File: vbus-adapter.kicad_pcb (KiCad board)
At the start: 2 copper layers, 76.5 x 49 mm, 32 parts, among them J1 VBUS, J2 CAN, J3 Screw_Terminal_01x03, J4 Screw_Terminal_01x03, J6 Backup GPIO, T800 AO3400A, U1 ISO7721D, U3 MCP2562-E-SN, U4 WeMos_S2_mini

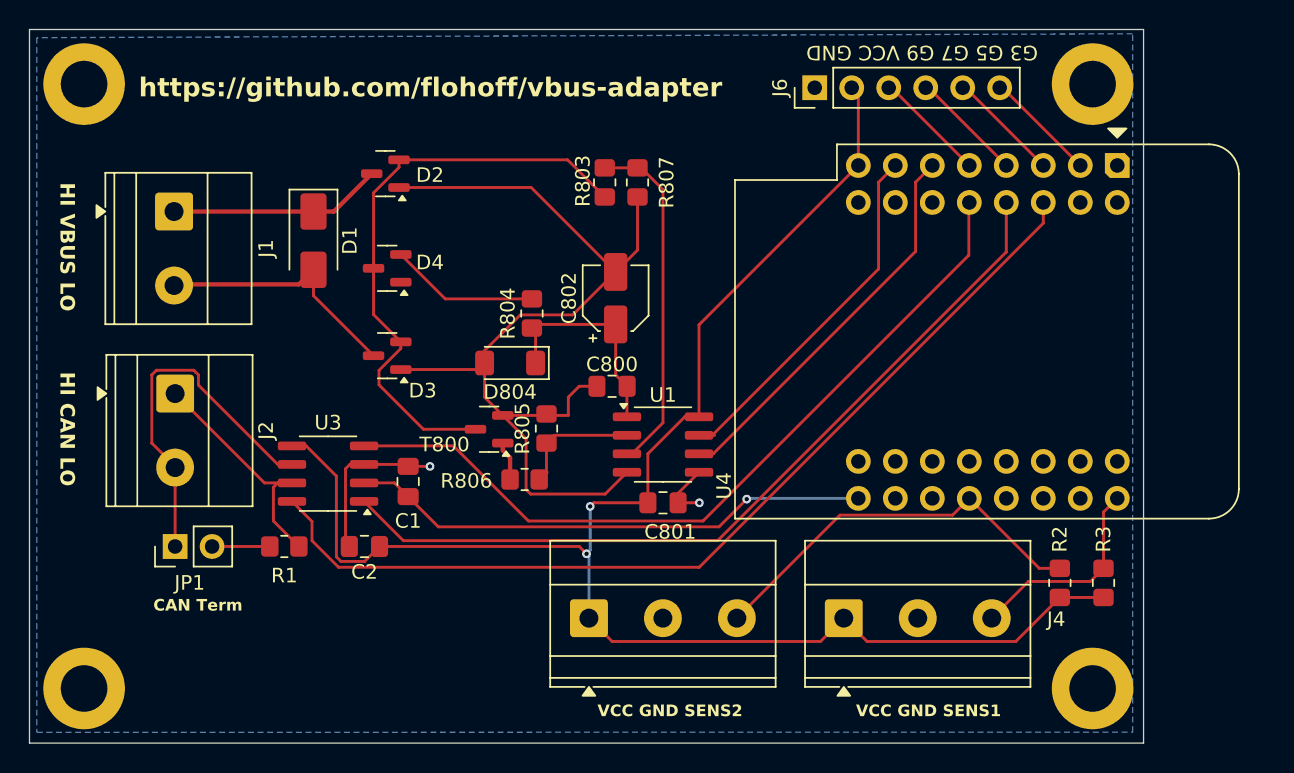
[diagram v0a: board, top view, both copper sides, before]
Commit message: Fix some issues
- Use ISO7721FDR (Default Low output) so on disconnect of
  the ESP32 (Power loss) the VBUS will not be pulled to low
  e.g. bus disabled.
- Add pull-down resistor to ISO input for TX
- Add VBUS r/w jumper disconnecting the MOSFet drain from the VBUS
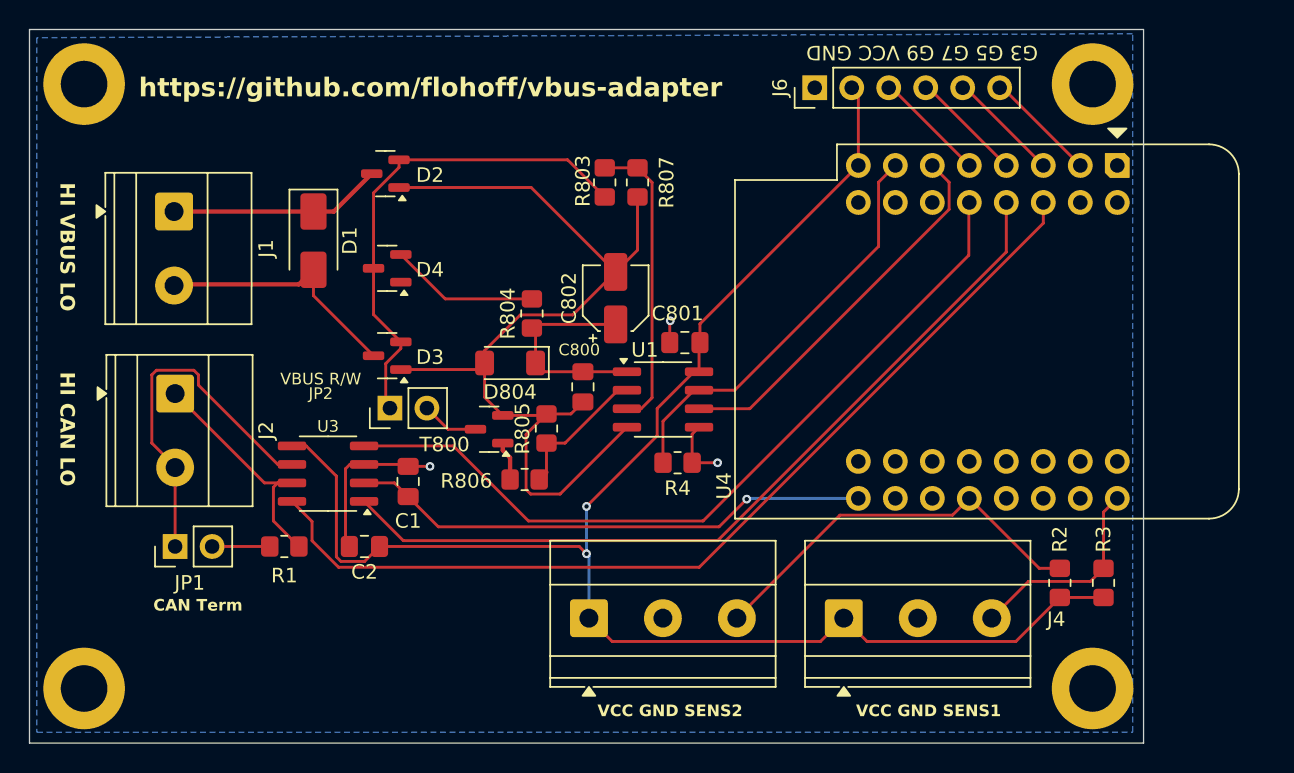
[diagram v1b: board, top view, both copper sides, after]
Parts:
- added JP2: VBUS R/W, Connector_PinHeader_2.54mm:PinHeader_1x02_P2.54mm_Vertical, F.Cu at (133.8, 99.0)
- added R4: 6k8, Resistor_SMD:R_0805_2012Metric_Pad1.20x1.40mm_HandSolder, F.Cu at (153.5, 102.8)
- U1: value ISO7721D -> ISO7721FDR
- moved C801 11.1 mm to (154.0, 94.5), turned to 180 degrees
- moved U1 3.09 mm to (152.5, 98.4)
- moved C800 2.00 mm to (147.0, 97.5), turned to -90 degrees
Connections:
- T800 pad 3: Net-(D2-K) -> Net-(JP2-B)
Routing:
- net Net-(D2-K): track 40.6 -> 34.3 mm
- net Net-(JP2-B): track 0.00 -> 3.94 mm
- net VBUS-IN: track 24.0 -> 20.5 mm
- net VBUS-MC-TX: track 25.7 -> 28.7 mm
- net VCC: track 113.1 -> 110.6 mm
- net GND: track 15.6 -> 17.3 mm, vias 2 -> 3
- net VBUS-OUT: track 9.15 -> 10.4 mm
- net VBUS-GND: track 66.7 -> 65.8 mm
- net VBUS-MC-RX: track 27.0 -> 26.3 mm

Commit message: Version 2
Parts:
- removed U4: WeMos_S2_mini, flo:WEMOS_S2_mini
- added C3: 10uF, Capacitor_SMD:C_0805_2012Metric_Pad1.18x1.45mm_HandSolder, F.Cu at (157.2, 77.2)
- added C4: 0.1uF, Capacitor_SMD:C_0805_2012Metric_Pad1.18x1.45mm_HandSolder, F.Cu at (154.7, 77.2)
- added C5: 0.1uF, Capacitor_SMD:C_0805_2012Metric_Pad1.18x1.45mm_HandSolder, F.Cu at (156.4, 82.0)
- added C6: 10uF, Capacitor_SMD:C_0805_2012Metric_Pad1.18x1.45mm_HandSolder, F.Cu at (161.4, 82.0)
- added C7: 10nF, Capacitor_SMD:C_0805_2012Metric_Pad1.18x1.45mm_HandSolder, F.Cu at (158.9, 82.0)
- added J5: Power, TerminalBlock_Phoenix:TerminalBlock_Phoenix_MPT-0,5-2-2.54_1x02_P2.54mm_Horizontal, F.Cu at (119.3, 115.1)
- added J7: Program, Connector_PinHeader_2.54mm:PinHeader_1x05_P2.54mm_Vertical, F.Cu at (154.4, 108.7)
- added Q1: SS8050, Package_TO_SOT_SMD:SOT-23, F.Cu at (167.8, 112.4)
- added Q2: SS8050, Package_TO_SOT_SMD:SOT-23, F.Cu at (158.2, 112.5)
- added R5: 10K, Resistor_SMD:R_0805_2012Metric_Pad1.20x1.40mm_HandSolder, F.Cu at (164.4, 112.6)
- added R6: 10K, Resistor_SMD:R_0805_2012Metric_Pad1.20x1.40mm_HandSolder, F.Cu at (161.8, 112.6)
- added U2: ESP32-S2-SOLO, PCM_Espressif:ESP32-S2-SOLO, F.Cu at (175.7, 93.8)
- added U5: SPX3819M5-L-3-3, Package_TO_SOT_SMD:SOT-23-5, F.Cu at (160.7, 77.3)
- J1, J2: footprint TerminalBlock_Phoenix:TerminalBlock_Phoenix_MKDS-1,5-2-5.08_1x02_P5.08mm_Horizontal -> TerminalBlock_Phoenix:TerminalBlock_Phoenix_MPT-0,5-2-2.54_1x02_P2.54mm_Horizontal
- J3: value Screw_Terminal_01x03 -> Sens 2; footprint TerminalBlock_Phoenix:TerminalBlock_Phoenix_MKDS-1,5-3-5.08_1x03_P5.08mm_Horizontal -> TerminalBlock_Phoenix:TerminalBlock_Phoenix_MPT-0,5-3-2.54_1x03_P2.54mm_Horizontal
- J4: value Screw_Terminal_01x03 -> Sens 1; footprint TerminalBlock_Phoenix:TerminalBlock_Phoenix_MKDS-1,5-3-5.08_1x03_P5.08mm_Horizontal -> TerminalBlock_Phoenix:TerminalBlock_Phoenix_MPT-0,5-3-2.54_1x03_P2.54mm_Horizontal
- moved R3 43.3 mm to (139.7, 115.3)
- moved R2 43.1 mm to (136.9, 115.3)
- moved J6 40.3 mm to (163.7, 117.3)
- moved C2 27.2 mm to (128.4, 81.5), turned to 0 degrees
- moved J4 21.7 mm to (143.3, 115.1)
- moved D2 21.1 mm to (129.3, 103.6)
- moved J3 19.7 mm to (127.8, 115.1)
- moved R1 18.9 mm to (122.4, 90.0), turned to 90 degrees
- moved C1 18.5 mm to (133.8, 85.6)
- moved U3 18.1 mm to (128.1, 85.5)
- moved J1 17.7 mm to (116.6, 103.1)
- moved JP1 17.7 mm to (116.6, 91.0)
- moved D1 17.3 mm to (124.4, 104.3)
- moved J2 13.9 mm to (116.5, 84.3)
- moved D3 12.6 mm to (129.4, 107.3)
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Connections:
- J6 pad 3: GPIO9 -> EXT1
- J6 pad 4: GPIO7 -> EXT2
- J6 pad 5: GPIO5 -> EXT3
- J6 pad 6: GPIO3 -> EXT4
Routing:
- net +5V: track 36.0 -> 107.6 mm, vias 1 -> 0
- net GND: track 17.3 -> 82.5 mm, vias 3 -> 8
- net VCC: track 110.6 -> 171.0 mm, vias 2 -> 3
- net EN: track 0.00 -> 37.3 mm, vias 0 -> 2
- net PROG_RXD: track 0.00 -> 25.4 mm, vias 0 -> 1
- net PROG_TXD: track 0.00 -> 24.2 mm, vias 0 -> 1
- net GPIO-SENS1: track 14.3 -> 36.7 mm
- net PROG: track 0.00 -> 20.6 mm
- net EXT1: track 0.00 -> 15.8 mm
- net EXT4: track 0.00 -> 15.3 mm
- net EXT2: track 0.00 -> 15.3 mm
- net EXT3: track 0.00 -> 14.8 mm
- net VBUS-MC-TX: track 28.7 -> 15.2 mm
- net GPIO-SENS2: track 27.6 -> 39.8 mm
- net VBUS-MC-RX: track 26.3 -> 15.0 mm
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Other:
- board text added: "${PROJECTNAME} ${REVISION} ${ISSUE_DATE}"
- board text added: "+5V GND"
- board text added: "GND RX TX RTS DTR"
- board text added: "GND VCC E1 E2 E3 E4"
- board text removed: "G3 G5 G7 G9 VCC GND"

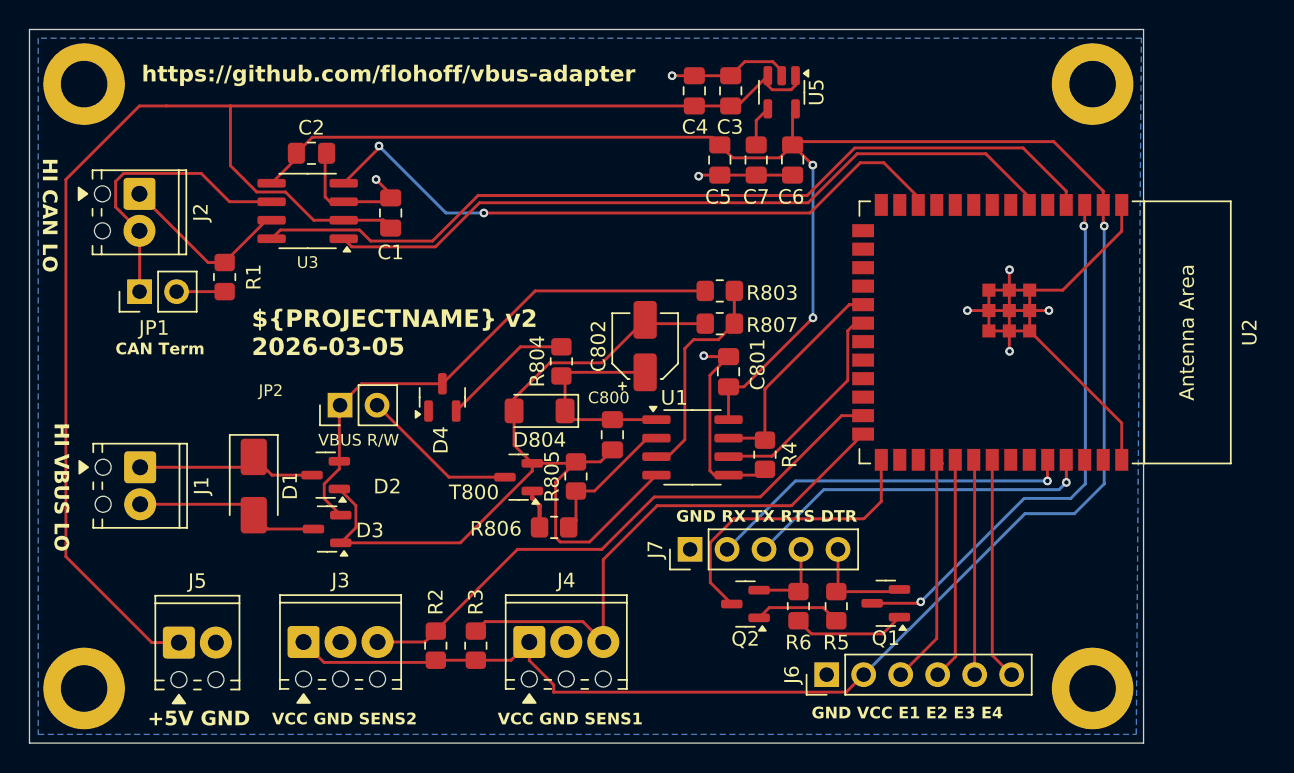
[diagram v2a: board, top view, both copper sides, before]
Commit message: Version 3 - Move GPIO for SENS, Add PWR/WIFI LED
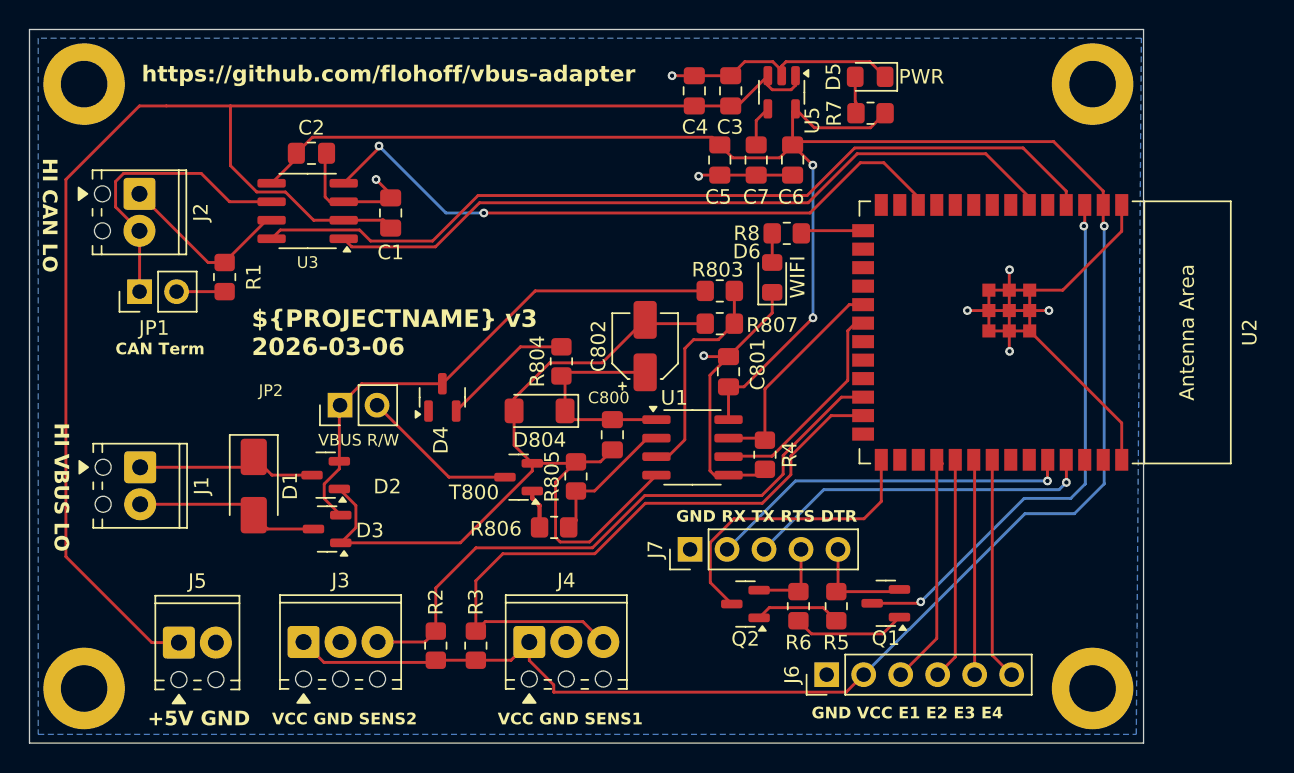
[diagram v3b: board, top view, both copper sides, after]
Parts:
- added D5: PWR, LED_SMD:LED_0805_2012Metric_Pad1.15x1.40mm_HandSolder, F.Cu at (166.7, 76.2)
- added D6: WIFI, LED_SMD:LED_0805_2012Metric_Pad1.15x1.40mm_HandSolder, F.Cu at (160.0, 90.0)
- added R7: 330R, Resistor_SMD:R_0805_2012Metric_Pad1.20x1.40mm_HandSolder, F.Cu at (166.8, 78.8)
- added R8: 330R, Resistor_SMD:R_0805_2012Metric_Pad1.20x1.40mm_HandSolder, F.Cu at (161.0, 87.0)
- R2, R3: value 4.7k -> 4k7
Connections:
- U2 pad 15: unconnected-(U2-GPIO3/TOUCH3/ADC1_CH2-Pad15) -> WIFI_LED
- U2 pad 24: unconnected-(U2-SPIIO4/GPIO33/FSPIHD-Pad24) -> GPIO-SENS2
- U2 pad 25: GPIO-SENS2 -> GPIO-SENS1
- U2 pad 26: GPIO-SENS1 -> unconnected-(U2-GPIO45-Pad26)
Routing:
- net GND: track 82.5 -> 96.4 mm
- net GPIO-SENS1: track 36.7 -> 45.1 mm
- net VCC: track 171.0 -> 178.1 mm
- net WIFI_LED: track 0.00 -> 4.32 mm
- net GPIO-SENS2: track 39.8 -> 42.8 mm
- net Net-(D5-A): track 0.00 -> 2.52 mm
- net Net-(D6-A): track 0.00 -> 2.00 mm
